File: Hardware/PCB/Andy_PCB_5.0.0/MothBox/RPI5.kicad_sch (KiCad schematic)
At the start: 4 parts, among them U16 Female Inv Socket Pi 2.54-2*20, U18 RASPBERRY_PI_4B_4GB, U4 RASPBERRY_PI_4B_4GB, U5 RASPBERRY_PI_5

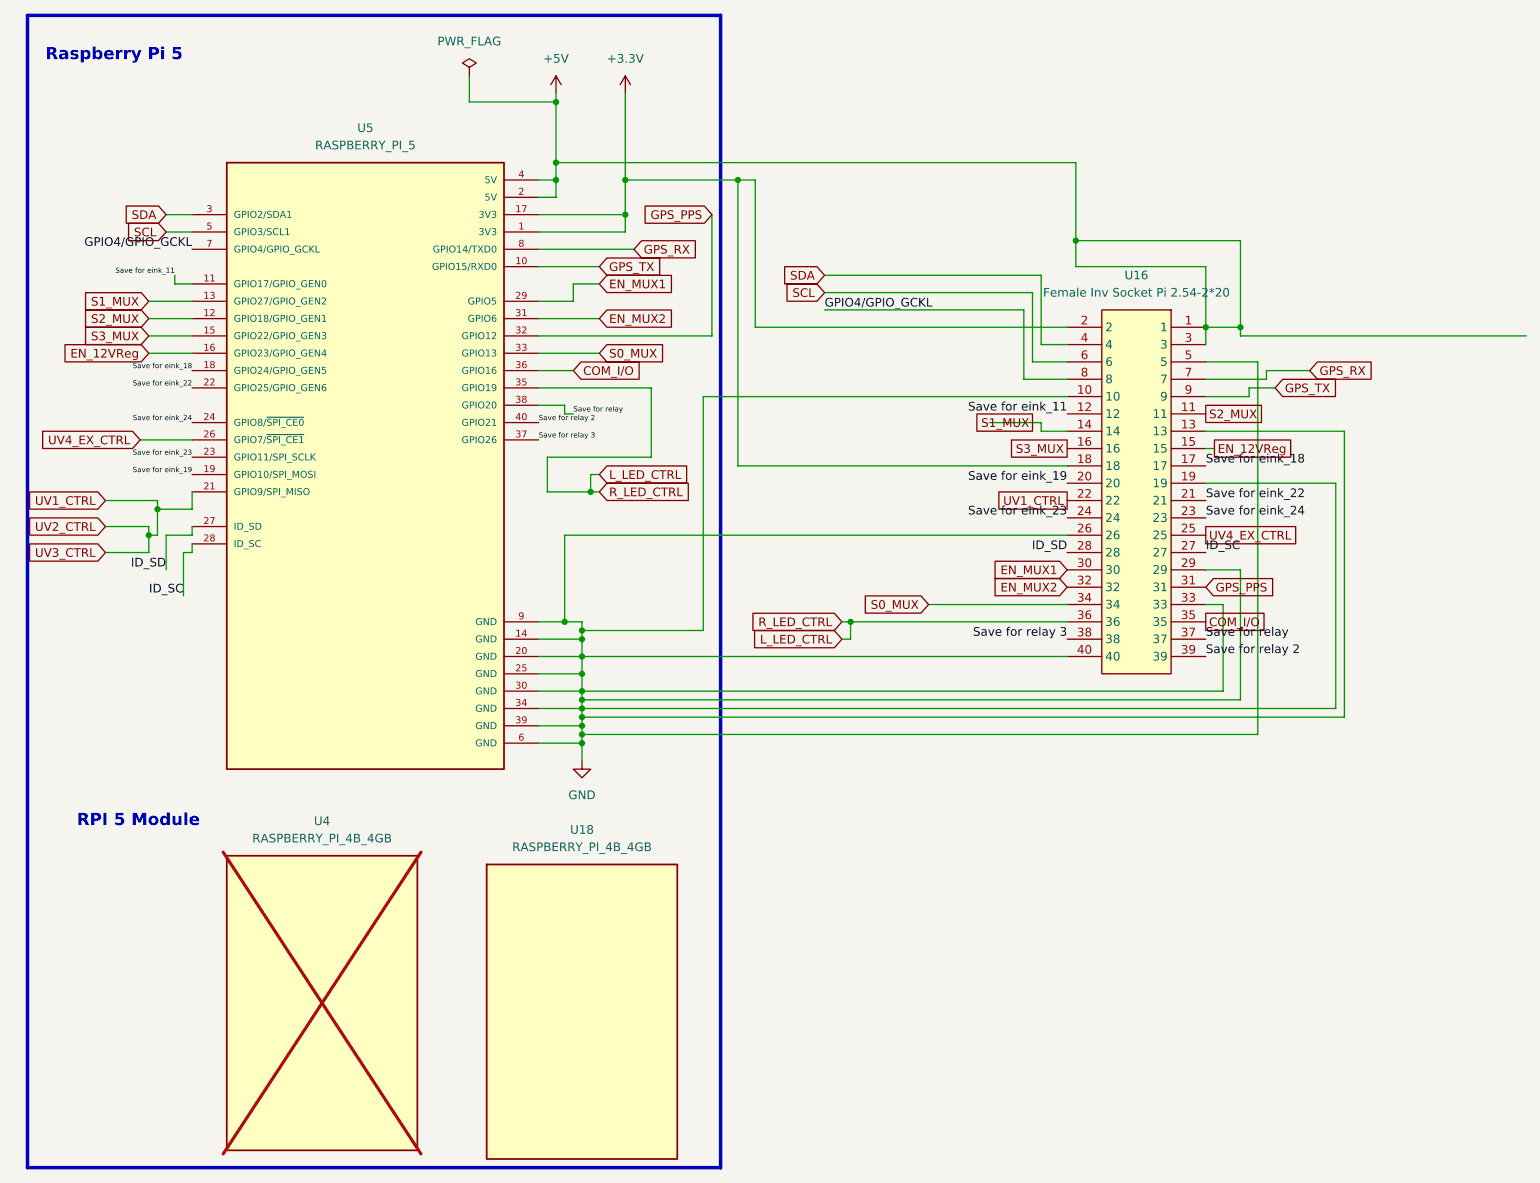
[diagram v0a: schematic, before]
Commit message: Moved Epaper and routed epaper and relay wires
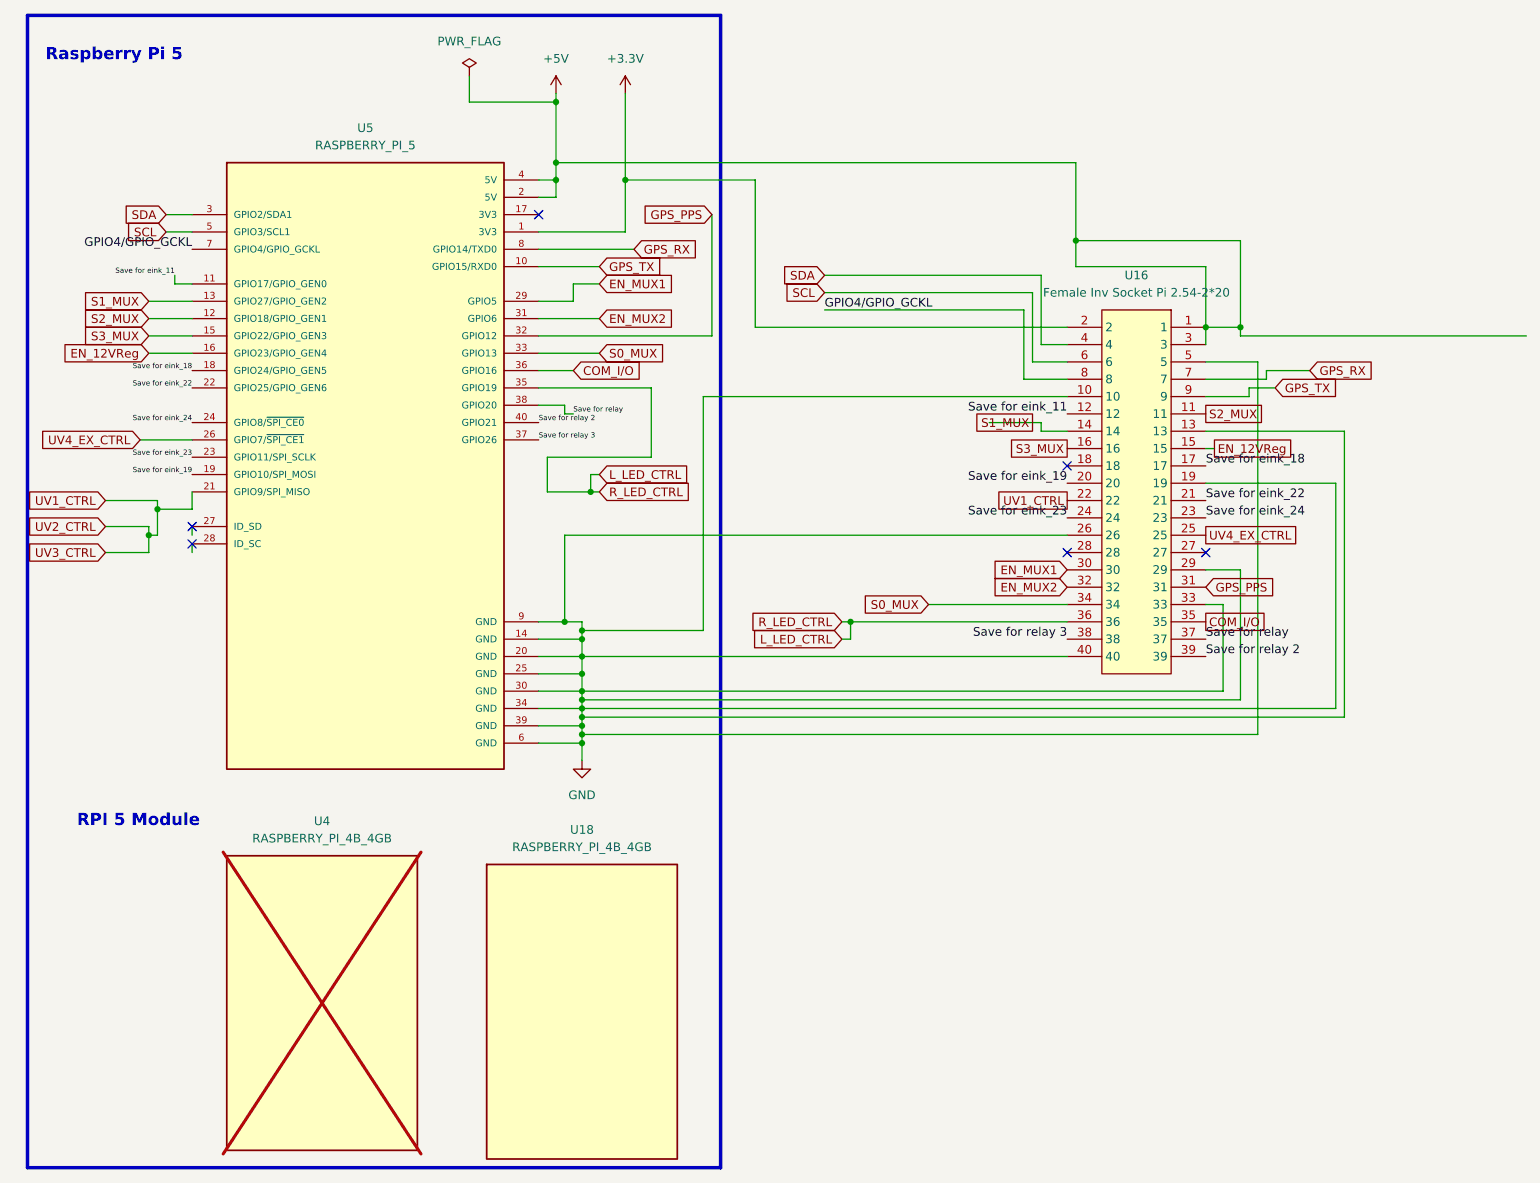
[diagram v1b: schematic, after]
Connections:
- net +3.3V: no longer U16.18, U5.17 (3V3)
- net ID_SC: no longer names the net of U5.28 (ID_SC)
- net ID_SC: no longer U16.27
- net ID_SD: no longer names the net of U5.27 (ID_SD)
- net ID_SD: no longer U16.28
- no-connect marks 0 -> 6
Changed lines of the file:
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@@
-	)
-	(junction
-		(at 125.73 40.64)
-		(diameter 0)
-		(color 0 0 0 0)
 	)
 	(junction
@@
 	)
 	(junction
-		(at 109.22 45.72)
-		(diameter 0)
-		(color 0 0 0 0)
-	)
-	(junction
 		(at 102.87 121.92)
 		(diameter 0)
@@
 		(color 0 0 0 0)
 	)
+	(no_connect
+		(at 45.72 93.98)
+	)
+	(no_connect
+		(at 96.52 45.72)
+	)
+	(no_connect
+		(at 173.99 82.55)
+	)
+	(no_connect
+		(at 45.72 91.44)
+	)
+	(no_connect
+		(at 194.31 95.25)
+	)
+	(no_connect
+		(at 173.99 95.25)
+	)
 	(wire
 		(pts
@@
 	(wire
 		(pts
-			(xy 125.73 82.55) (xy 125.73 40.64)
-		)
-		(stroke
-			(width 0)
-			(type default)
-		)
-	)
-	(wire
-		(pts
 			(xy 96.52 105.41) (xy 100.33 105.41)
 		)
@@
 	(wire
 		(pts
-			(xy 44.45 101.6) (xy 44.45 95.25)
-		)
-		(stroke
-			(width 0)
-			(type default)
-		)
-	)
-	(wire
-		(pts
 			(xy 201.93 67.31) (xy 201.93 121.92)
 		)
@@
 	(wire
 		(pts
-			(xy 173.99 82.55) (xy 125.73 82.55)
-		)
-		(stroke
-			(width 0)
-			(type default)
-		)
-	)
-	(wire
-		(pts
 			(xy 104.14 86.36) (xy 105.41 86.36)
 		)
@@
 	(wire
 		(pts
-			(xy 41.91 97.79) (xy 41.91 92.71)
-		)
-		(stroke
-			(width 0)
-			(type default)
-		)
-	)
-	(wire
-		(pts
 			(xy 120.65 106.68) (xy 102.87 106.68)
 		)
@@
 	(wire
 		(pts
-			(xy 96.52 45.72) (xy 109.22 45.72)
-		)
-		(stroke
-			(width 0)
-			(type default)
-		)
-	)
-	(wire
-		(pts
-			(xy 109.22 45.72) (xy 109.22 48.26)
-		)
-		(stroke
-			(width 0)
-			(type default)
-		)
-	)
-	(wire
-		(pts
 			(xy 41.91 45.72) (xy 45.72 45.72)
 		)
@@
 	(wire
 		(pts
-			(xy 109.22 40.64) (xy 109.22 45.72)
+			(xy 109.22 40.64) (xy 109.22 48.26)
 		)
 		(stroke
@@
 	(wire
 		(pts
-			(xy 128.27 40.64) (xy 125.73 40.64)
+			(xy 109.22 40.64) (xy 128.27 40.64)
 		)
 		(stroke
@@
 	(wire
 		(pts
-			(xy 125.73 40.64) (xy 109.22 40.64)
-		)
-		(stroke
-			(width 0)
-			(type default)
-		)
-	)
-	(wire
-		(pts
 			(xy 173.99 92.71) (xy 100.33 92.71)
 		)
@@
 	(wire
 		(pts
-			(xy 41.91 92.71) (xy 45.72 92.71)
-		)
-		(stroke
-			(width 0)
-			(type default)
-		)
-	)
-	(wire
-		(pts
 			(xy 33.02 87.63) (xy 40.64 87.63)
 		)
@@
 		(pts
 			(xy 41.91 48.26) (xy 45.72 48.26)
-		)
-		(stroke
-			(width 0)
-			(type default)
-		)
-	)
-	(wire
-		(pts
-			(xy 44.45 95.25) (xy 45.72 95.25)
 		)
 		(stroke
@@
 		)
 	)
-	(label "ID_SD"
-		(at 173.99 95.25 180)
-		(effects
-			(font
-				(size 1.27 1.27)
-			)
-			(justify right bottom)
-		)
-	)
 	(label "Save for relay 3"
 		(at 96.52 78.74 0)
@@
 		)
 	)
-	(label "ID_SC"
-		(at 44.45 101.6 180)
-		(effects
-			(font
-				(size 1.27 1.27)
-			)
-			(justify right bottom)
-		)
-	)
 	(label "Save for eink_11"
 		(at 43.18 54.61 180)
@@
 		)
 	)
-	(label "ID_SD"
-		(at 41.91 97.79 180)
-		(effects
-			(font
-				(size 1.27 1.27)
-			)
-			(justify right bottom)
-		)
-	)
 	(label "Save for eink_23"
 		(at 45.72 81.28 180)
@@
 		)
 	)
-	(label "ID_SC"
-		(at 194.31 95.25 0)
-		(effects
-			(font
-				(size 1.27 1.27)
-			)
-			(justify left bottom)
-		)
-	)

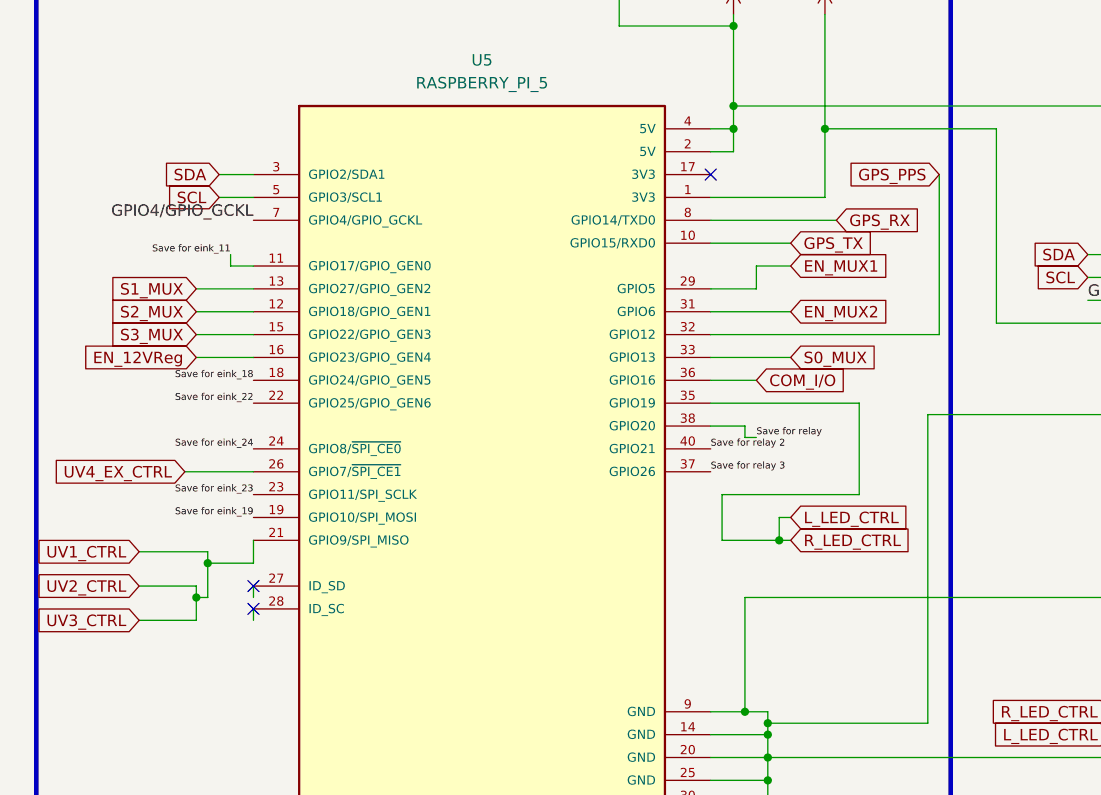
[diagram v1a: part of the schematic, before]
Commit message: Multiplexers wired together
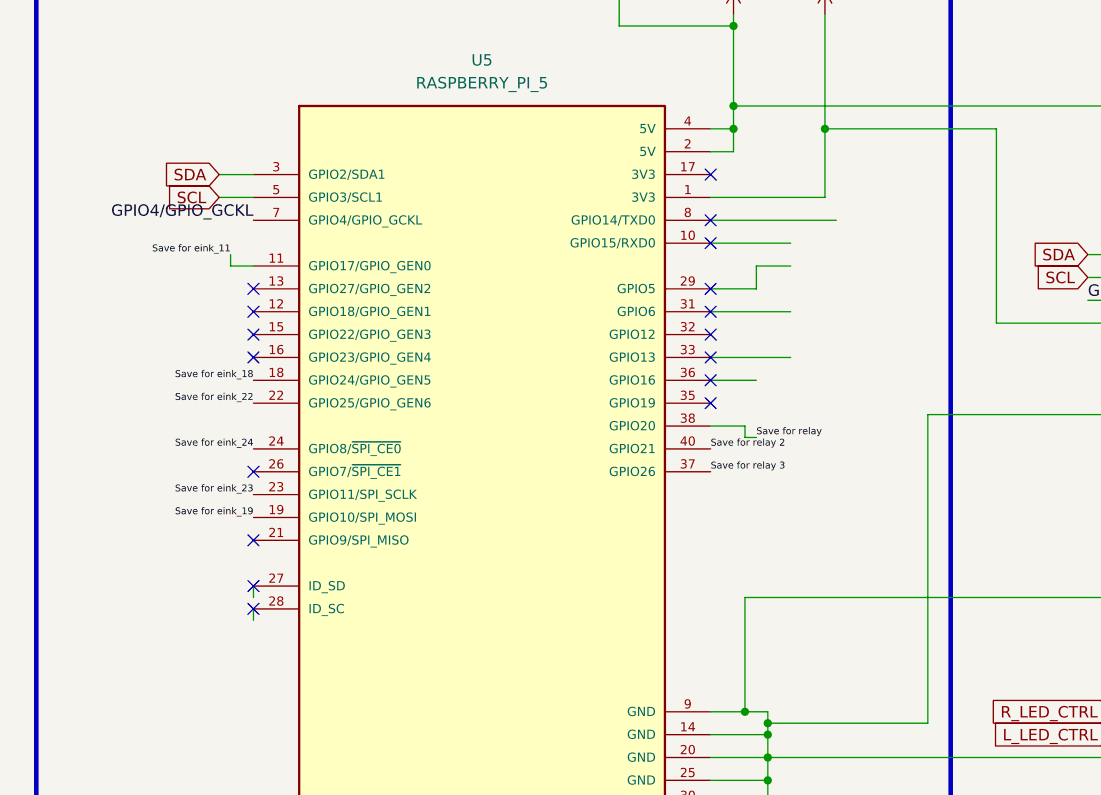
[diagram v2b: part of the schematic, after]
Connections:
- net COM_I/O: no longer U5.36 (GPIO16)
- net EN_12VReg: no longer U5.16 (GPIO23/GPIO_GEN4)
- net EN_MUX1: no longer U5.29 (GPIO5)
- net EN_MUX2: no longer U5.31 (GPIO6)
- net GPS_PPS: no longer U5.32 (GPIO12)
- net GPS_RX: no longer U5.8 (GPIO14/TXD0)
- net GPS_TX: no longer U5.10 (GPIO15/RXD0)
- net L_LED_CTRL: no longer U5.35 (GPIO19)
- net S0_MUX: no longer U5.33 (GPIO13)
- net S1_MUX: no longer U5.13 (GPIO27/GPIO_GEN2)
- net S2_MUX: no longer U5.12 (GPIO18/GPIO_GEN1)
- net S3_MUX: no longer U5.15 (GPIO22/GPIO_GEN3)
- net UV1_CTRL: no longer U5.21 (GPIO9/SPI_MISO)
- net UV4_EX_CTRL: no longer U5.26 (GPIO7/~{SPI_CE1})
- no-connect marks 6 -> 20

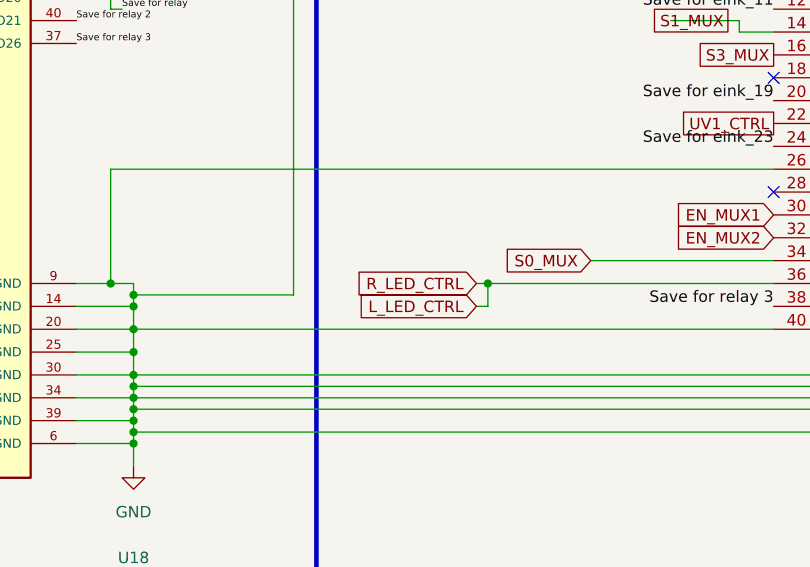
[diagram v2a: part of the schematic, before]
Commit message: Almost everything wired up
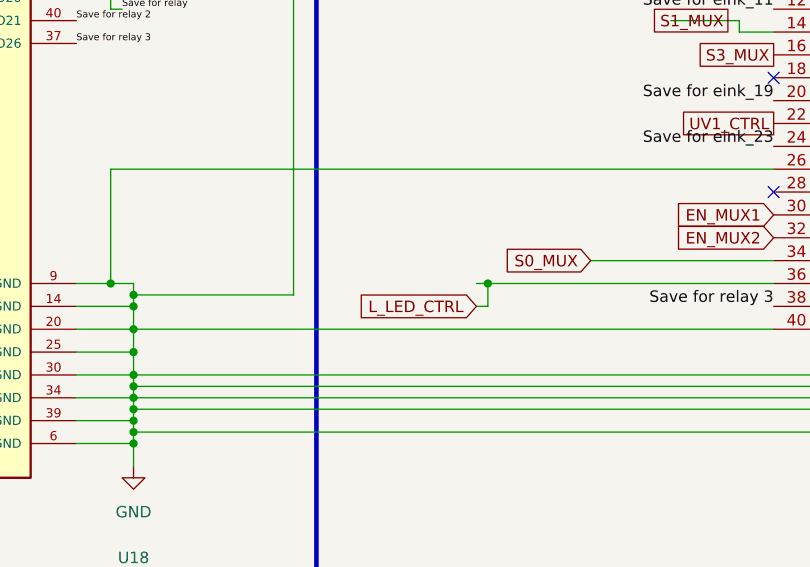
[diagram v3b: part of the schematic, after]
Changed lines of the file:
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@@
-		)
-	)
-	(global_label "R_LED_CTRL"
-		(shape input)
-		(at 140.97 105.41 180)
-		(fields_autoplaced yes)
-		(effects
-			(font
-				(size 1.27 1.27)
-			)
-			(justify right)
-		)
-		(property "Intersheetrefs" "${INTERSHEET_REFS}"
-			(at 126.7968 105.41 0)
-			(effects
-				(font
-					(size 1.27 1.27)
-				)
-				(justify right)
-				(hide yes)
-			)
 		)
 	)

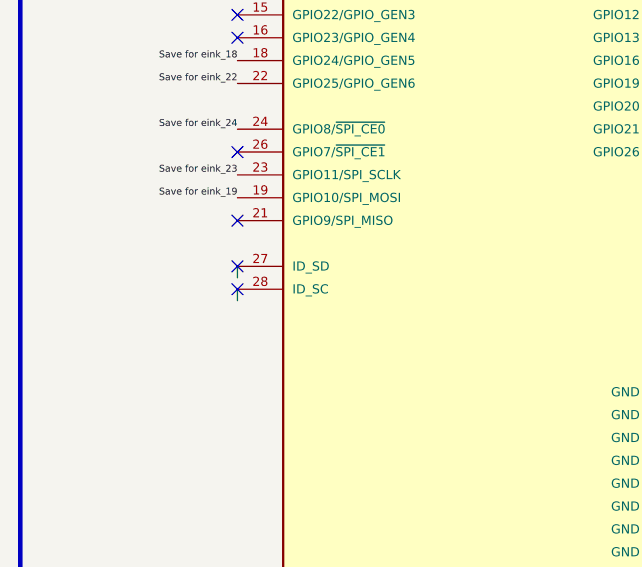
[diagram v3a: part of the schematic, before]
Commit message: cleaned most schematic and got rid of half errors in ERC
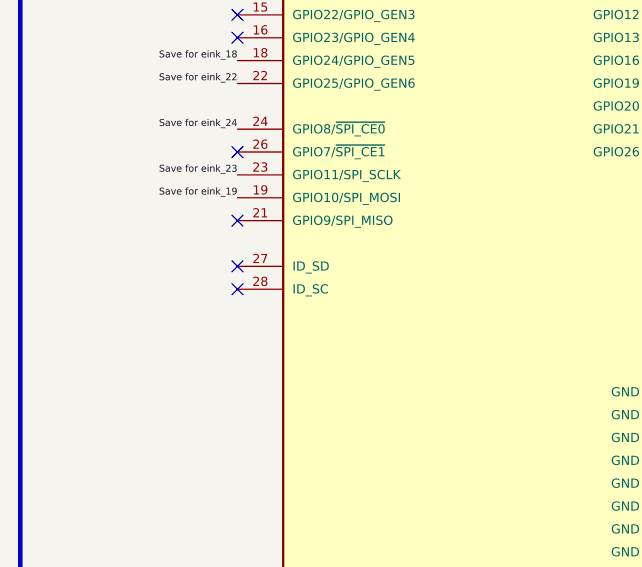
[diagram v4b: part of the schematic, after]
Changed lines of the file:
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@@
-	(wire
-		(pts
-			(xy 45.72 95.25) (xy 45.72 93.98)
-		)
-		(stroke
-			(width 0)
-			(type default)
-		)
-	)
 	(wire
 		(pts
@@
 		)
 		(stroke
-			(width 0)
-			(type default)
-		)
-	)
-	(wire
-		(pts
-			(xy 45.72 92.71) (xy 45.72 91.44)
-		)
-		(stroke
